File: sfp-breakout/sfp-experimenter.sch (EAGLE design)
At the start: 51 parts, among them IC1 SN65LVDS1DBV, IC2 SN65LVDT2DBV, J1 PJ-002BH-SMT-TR, T1 BC847, T2 BC847, U1 LDO-MCP1825S, X1 PINHD-1X5LOCK, X2 PINHD-1X5LOCK, X3 PINHD-1X4LOCK

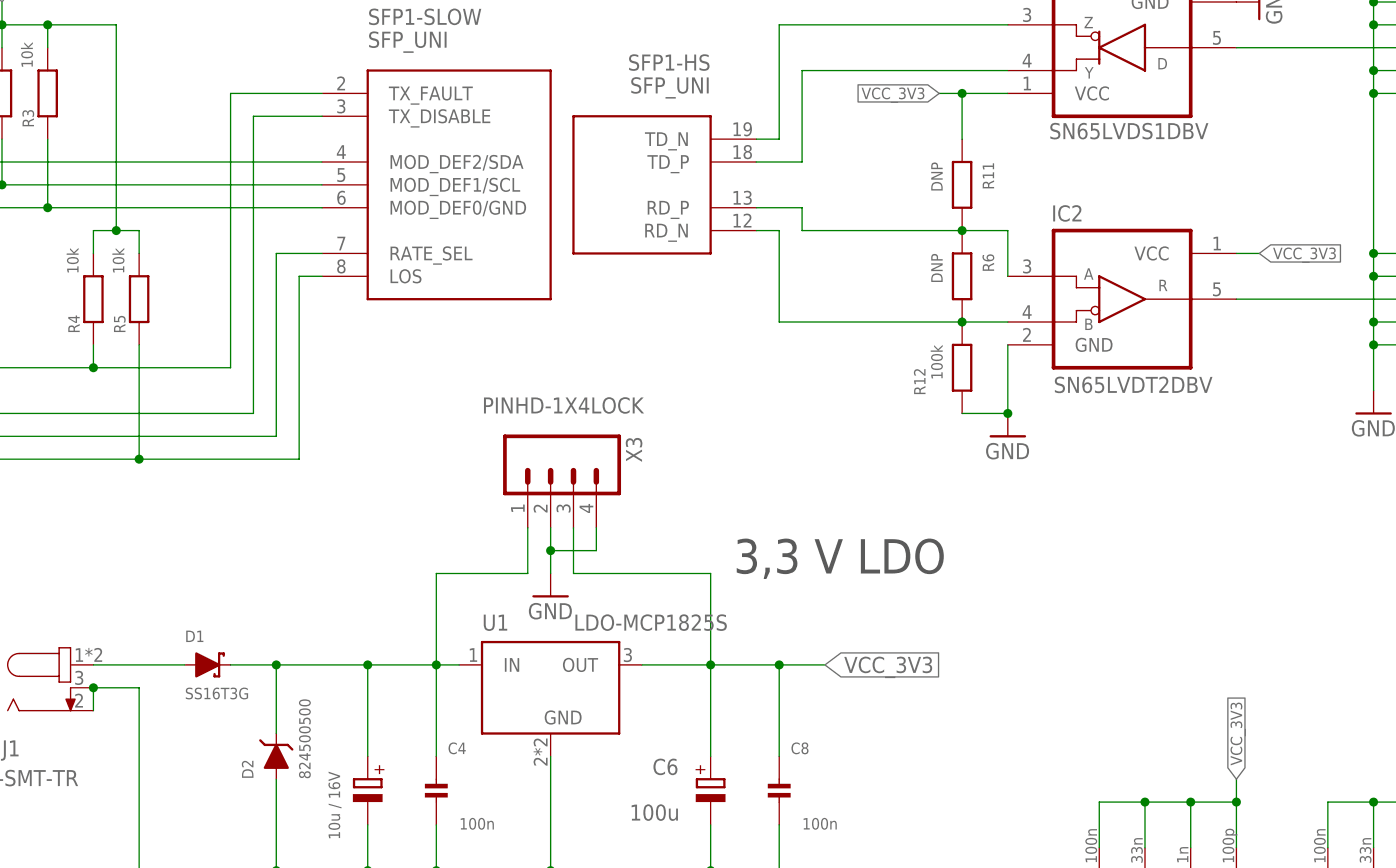
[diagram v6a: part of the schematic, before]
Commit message: sfp-experimenter: update ext BOM attr to newer Digikey format
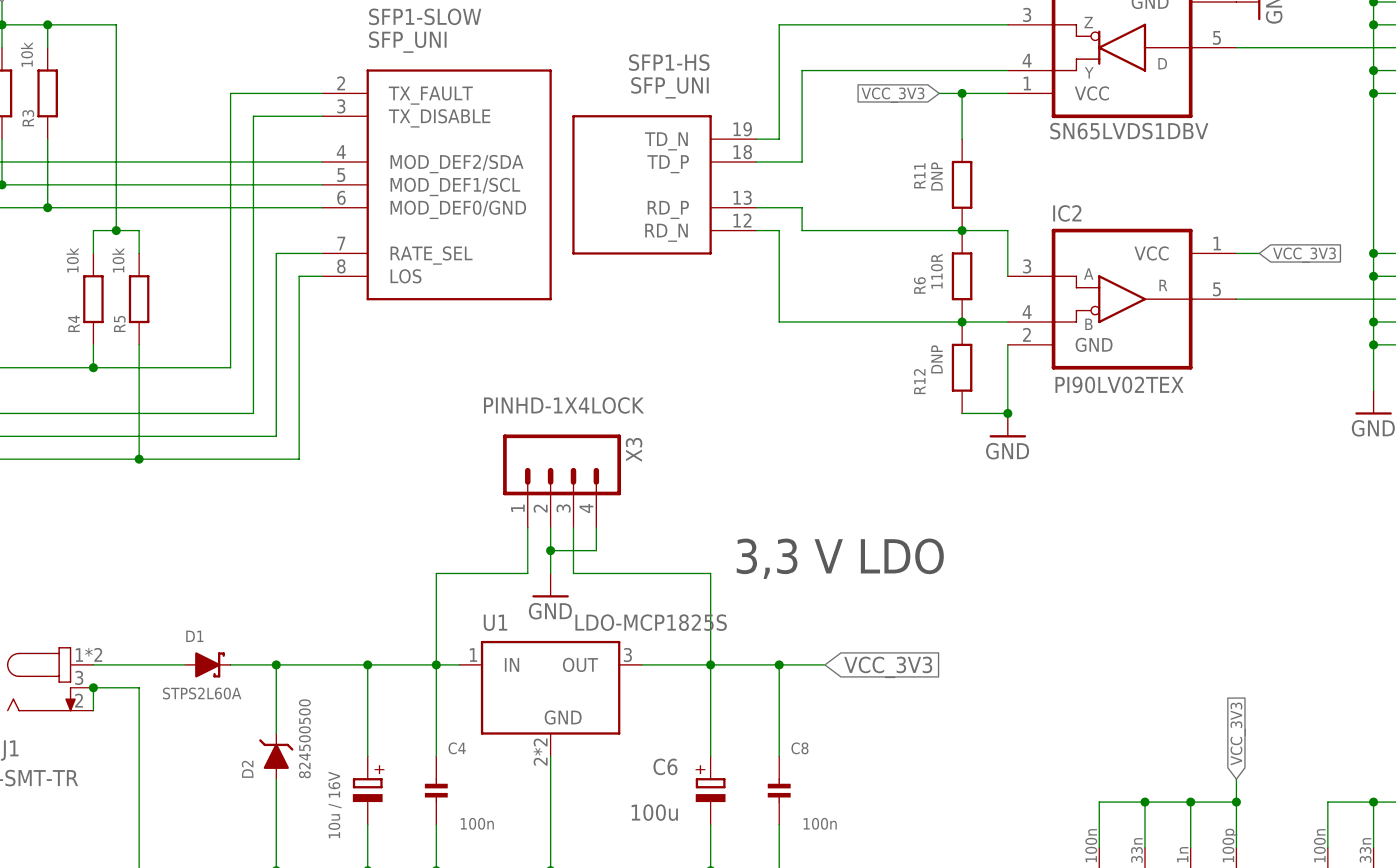
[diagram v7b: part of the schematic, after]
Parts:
- D1: value SS16T3G -> STPS2L60A
- IC2: value SN65LVDT2DBV -> PI90LV02TEX; DATASHEET http://www.ti.com/general/docs/suppproductinfo.tsp?distId=1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 -> https://www.diodes.com/assets/Datasheets/PI90LV02.pdf; LINK https://www.digikey.com/product-detail/en/texas-instruments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 -> https://www.digikey.com/en/products/detail/diodes-incorpora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; MANUFACTURER Texas Instruments -> Diodes Incorporated; MANUFACTURERPARTNUMBER SN65LVDT2DBVR -> PI90LV02TEX; SOURCEPARTNUMBER 296-6896-1-ND -> PI90LV02TEXCT-ND
- R12: value 100k -> DNP; POPULATED TRUE -> FALSE
- R6: value DNP -> 110R; DATASHEET (none) -> https://www.yageo.com/upload/media/product/productsearch/da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; DESCRIPTION NO DESCRIPTION -> RES 110 OHM 1% 1/10W 0603; LINK UNKNOWN LINK -> https://www.digikey.com/en/products/detail/yageo/RC0603FR-1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; MANUFACTURER UNKNOWN MANUFACTURER -> YAGEO; MANUFACTURERPARTNUMBER UNKNOWN MANUFACTURER PART NUMBER -> RC0603FR-13110RL; POPULATED FALSE -> TRUE; ROHSCERTIFICATE UNKNOWN ROHS CERTIFICATE -> ROHS3 Compliant; SOURCE UNKNOWN SOURCE -> DIGIKEY; SOURCEPARTNUMBER UNKNOWN SOURCE PART NUMBER -> 13-RC0603FR-13110RLCT-ND
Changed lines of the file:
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@@
 <part name="GND10" library="sfp-experimenter" deviceset="GND" device=""/>
 <part name="GND13" library="sfp-experimenter" deviceset="GND" device=""/>
-<part name="IC2" library="sfp-experimenter" deviceset="SN65LVDT2" device="DBV" value="SN65LVDT2DBV">
+<part name="IC2" library="sfp-experimenter" deviceset="SN65LVDT2" device="DBV" value="PI90LV02TEX">
 <attribute name="CLASS" value="IC"/>
-<attribute name="DATASHEET" value="http://www.ti.com/general/docs/suppproductinfo.tsp?distId=10&amp;gotoUrl=http%3A%2F%2Fwww.ti.com%2Flit%2Fgpn%2Fsn65lvds1"/>
+<attribute name="DATASHEET" value="https://www.diodes.com/assets/Datasheets/PI90LV02.pdf"/>
 <attribute name="DESCRIPTION" value="IC RECEIVER 0/1 SOT23-5"/>
-<attribute name="LINK" value="https://www.digikey.com/product-detail/en/texas-instruments/SN65LVDT2DBVR/296-6896-1-ND/371534"/>
-<attribute name="MANUFACTURER" value="Texas Instruments"/>
-<attribute name="MANUFACTURERPARTNUMBER" value="SN65LVDT2DBVR"/>
-<attribute name="POPULATED" value="TRUE"/>
-<attribute name="ROHSCERTIFICATE" value="ROHS3 Compliant"/>
-<attribute name="SOURCE" value="DIGIKEY"/>
-<attribute name="SOURCEPARTNUMBER" value="296-6896-1-ND"/>
+<attribute name="LINK" value="https://www.digikey.com/en/products/detail/diodes-incorporated/PI90LV02TEX/1142813"/>
+<attribute name="MANUFACTURER" value="Diodes Incorporated"/>
+<attribute name="MANUFACTURERPARTNUMBER" value="PI90LV02TEX"/>
+<attribute name="POPULATED" value="TRUE"/>
+<attribute name="ROHSCERTIFICATE" value="ROHS3 Compliant"/>
+<attribute name="SOURCE" value="DIGIKEY"/>
+<attribute name="SOURCEPARTNUMBER" value="PI90LV02TEXCT-ND"/>
 </part>
 <part name="IC1" library="sfp-experimenter" deviceset="SN65LVDS1" device="DBV">
@@
 <attribute name="SOURCEPARTNUMBER" value="MCP1825ST-3302E/DBCT-ND"/>
 </part>
-<part name="D1" library="sfp-experimenter" deviceset="DIODE-SCHOTTKY" device="-SMA" value="SS16T3G">
+<part name="D1" library="sfp-experimenter" deviceset="DIODE-SCHOTTKY" device="-SMA" value="STPS2L60A">
 <attribute name="CLASS" value="DIODE"/>
 <attribute name="DATASHEET" value="https://www.st.com/content/ccc/resource/technical/document/datasheet/b7/ac/e1/7d/2a/e9/4b/e8/CD00003166.pdf/files/CD00003166.pdf/jcr:content/translations/en.CD00003166.pdf"/>
@@
 <attribute name="SOURCEPARTNUMBER" value="SMAJ5.0ABCT-ND"/>
 </part>
-<part name="R6" library="sfp-experimenter" deviceset="RESISTOR" device="_0402" value="DNP">
+<part name="R6" library="sfp-experimenter" deviceset="RESISTOR" device="_0402" value="110R">
 <attribute name="CLASS" value="RESISTOR"/>
-<attribute name="DESCRIPTION" value="NO DESCRIPTION"/>
-<attribute name="LINK" value="UNKNOWN LINK"/>
-<attribute name="MANUFACTURER" value="UNKNOWN MANUFACTURER"/>
-<attribute name="MANUFACTURERPARTNUMBER" value="UNKNOWN MANUFACTURER PART NUMBER"/>
-<attribute name="POPULATED" value="FALSE"/>
-<attribute name="ROHSCERTIFICATE" value="UNKNOWN ROHS CERTIFICATE"/>
-<attribute name="SOURCE" value="UNKNOWN SOURCE"/>
-<attribute name="SOURCEPARTNUMBER" value="UNKNOWN SOURCE PART NUMBER"/>
+<attribute name="DATASHEET" value="https://www.yageo.com/upload/media/product/productsearch/datasheet/rchip/PYu-RC_Group_51_RoHS_L_12.pdf"/>
+<attribute name="DESCRIPTION" value="RES 110 OHM 1% 1/10W 0603"/>
+<attribute name="LINK" value="https://www.digikey.com/en/products/detail/yageo/RC0603FR-13110RL/14286378"/>
+<attribute name="MANUFACTURER" value="YAGEO"/>
+<attribute name="MANUFACTURERPARTNUMBER" value="RC0603FR-13110RL"/>
+<attribute name="POPULATED" value="TRUE"/>
+<attribute name="ROHSCERTIFICATE" value="ROHS3 Compliant"/>
+<attribute name="SOURCE" value="DIGIKEY"/>
+<attribute name="SOURCEPARTNUMBER" value="13-RC0603FR-13110RLCT-ND"/>
 </part>
 <part name="X3" library="sfp-experimenter" deviceset="PINHD-1X4" device="LOCK">
@@
 </part>
 <part name="GND22" library="sfp-experimenter" deviceset="GND" device=""/>
-<part name="R12" library="rc-sysmocom" deviceset="RESISTOR" device="_0603" value="100k">
+<part name="R12" library="rc-sysmocom" deviceset="RESISTOR" device="_0603" value="DNP">
 <attribute name="CLASS" value="RESISTOR"/>
 <attribute name="DATASHEET" value="https://www.koaspeer.com/pdfs/RK73H.pdf"/>
@@
 <attribute name="MANUFACTURER" value="KOA Speer Electronics, Inc."/>
 <attribute name="MANUFACTURERPARTNUMBER" value="RK73H1JTTD1003F"/>
-<attribute name="POPULATED" value="TRUE"/>
+<attribute name="POPULATED" value="FALSE"/>
 <attribute name="ROHSCERTIFICATE" value="ROHS3 Compliant"/>
 <attribute name="SOURCE" value="DIGIKEY"/>
@@
 <attribute name="NAME" x="154.686" y="135.636" size="1.778" layer="95" ratio="10"/>
 <attribute name="VALUE" x="154.94" y="116.586" size="1.778" layer="96" ratio="10"/>
-<attribute name="DESCRIPTION" x="162.56" y="127" size="1.27" layer="96" display="off"/>
-<attribute name="MANUFACTURER" x="162.56" y="127" size="1.27" layer="96" display="off"/>
-<attribute name="MANUFACTURERPARTNUMBER" x="162.56" y="127" size="1.27" layer="96" display="off"/>
-<attribute name="SOURCE" x="162.56" y="127" size="1.27" layer="96" display="off"/>
-<attribute name="SOURCEPARTNUMBER" x="162.56" y="127" size="1.27" layer="96" display="off"/>
-<attribute name="ROHSCERTIFICATE" x="162.56" y="127" size="1.27" layer="96" display="off"/>
-<attribute name="POPULATED" x="162.56" y="127" size="1.27" layer="96" display="off"/>
-<attribute name="CLASS" x="162.56" y="127" size="1.27" layer="96" display="off"/>
-<attribute name="LINK" x="162.56" y="127" size="1.27" layer="96" display="off"/>
+<attribute name="DESCRIPTION" x="162.56" y="127" size="1.778" layer="96" rot="R270" display="off"/>
+<attribute name="MANUFACTURER" x="162.56" y="127" size="1.778" layer="96" rot="R270" display="off"/>
+<attribute name="MANUFACTURERPARTNUMBER" x="162.56" y="127" size="1.778" layer="96" rot="R270" display="off"/>
+<attribute name="SOURCE" x="162.56" y="127" size="1.778" layer="96" rot="R270" display="off"/>
+<attribute name="SOURCEPARTNUMBER" x="162.56" y="127" size="1.778" layer="96" rot="R270" display="off"/>
+<attribute name="ROHSCERTIFICATE" x="162.56" y="127" size="1.778" layer="96" rot="R270" display="off"/>
+<attribute name="POPULATED" x="162.56" y="127" size="1.778" layer="96" rot="R270" display="off"/>
+<attribute name="CLASS" x="162.56" y="127" size="1.778" layer="96" rot="R270" display="off"/>
+<attribute name="LINK" x="162.56" y="127" size="1.778" layer="96" rot="R270" display="off"/>
 </instance>
 <instance part="IC1" gate="A" x="162.56" y="154.94" smashed="yes" rot="R180">
@@
 <attribute name="LINK" x="99.06" y="83.82" size="1.778" layer="96" display="off"/>
 </instance>
-<instance part="D1" gate="G$1" x="60.96" y="86.36">
+<instance part="D1" gate="G$1" x="60.96" y="86.36" smashed="yes">
 <attribute name="DESCRIPTION" x="60.96" y="86.36" size="1.778" layer="96" display="off"/>
 <attribute name="MANUFACTURER" x="60.96" y="86.36" size="1.778" layer="96" display="off"/>
@@
 <attribute name="CLASS" x="60.96" y="86.36" size="1.778" layer="96" display="off"/>
 <attribute name="LINK" x="60.96" y="86.36" size="1.778" layer="96" display="off"/>
+<attribute name="NAME" x="58.42" y="88.9" size="1.27" layer="95"/>
+<attribute name="VALUE" x="55.88" y="82.55" size="1.27" layer="96"/>
 </instance>
 <instance part="D2" gate="G$1" x="68.58" y="76.2" rot="R90">
@@
 <attribute name="LINK" x="68.58" y="76.2" size="1.778" layer="96" display="off"/>
 </instance>
-<instance part="R6" gate="G$1" x="144.78" y="129.54" rot="R270">
+<instance part="R6" gate="G$1" x="144.78" y="129.54" smashed="yes" rot="R270">
 <attribute name="DESCRIPTION" x="144.78" y="129.54" size="1.778" layer="96" display="off"/>
 <attribute name="MANUFACTURER" x="144.78" y="129.54" size="1.778" layer="96" display="off"/>
@@
 <attribute name="CLASS" x="144.78" y="129.54" size="1.778" layer="96" display="off"/>
 <attribute name="LINK" x="144.78" y="129.54" size="1.778" layer="96" display="off"/>
+<attribute name="NAME" x="139.446" y="129.54" size="1.27" layer="95" rot="R270"/>
+<attribute name="VALUE" x="141.351" y="132.08" size="1.27" layer="96" rot="R270"/>
 </instance>
 <instance part="X3" gate="G$1" x="99.06" y="109.22" smashed="yes" rot="R270">
@@
 <attribute name="LINK" x="144.78" y="119.38" size="1.778" layer="96" display="off"/>
 </instance>
-<instance part="R11" gate="G$1" x="144.78" y="139.7" rot="R270">
+<instance part="R11" gate="G$1" x="144.78" y="139.7" smashed="yes" rot="R270">
 <attribute name="DESCRIPTION" x="144.78" y="139.7" size="1.778" layer="96" display="off"/>
 <attribute name="MANUFACTURER" x="144.78" y="139.7" size="1.778" layer="96" display="off"/>
@@
 <attribute name="CLASS" x="144.78" y="139.7" size="1.778" layer="96" display="off"/>
 <attribute name="LINK" x="144.78" y="139.7" size="1.778" layer="96" display="off"/>
+<attribute name="NAME" x="139.446" y="142.24" size="1.27" layer="95" rot="R270"/>
+<attribute name="VALUE" x="141.351" y="142.24" size="1.27" layer="96" rot="R270"/>
 </instance>
 <instance part="M1" gate="G$1" x="167.64" y="33.02"/>

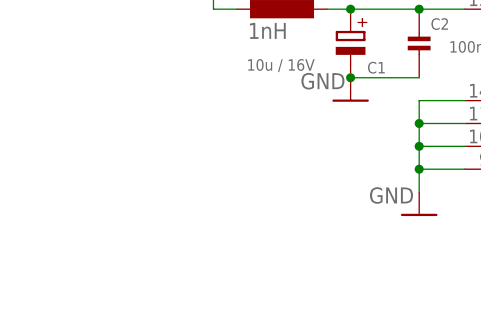
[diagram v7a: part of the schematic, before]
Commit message: sfp-experimenter: insert main fiducials
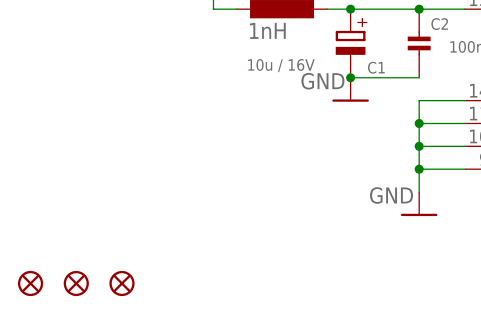
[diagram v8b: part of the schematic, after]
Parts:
- added FID1, FID2, FID3: FIDUCIAL1X2.5, microbuilder:FIDUCIAL1X2.5
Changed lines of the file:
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@@
 <layer number="99" name="position" color="7" fill="9" visible="no" active="yes"/>
 <layer number="100" name="Muster" color="7" fill="1" visible="no" active="no"/>
+<layer number="101" name="Patch_Top" color="12" fill="4" visible="yes" active="yes"/>
+<layer number="102" name="Mittellin" color="7" fill="1" visible="yes" active="yes"/>
+<layer number="103" name="Stiffner" color="7" fill="1" visible="yes" active="yes"/>
+<layer number="104" name="Name" color="7" fill="1" visible="yes" active="yes"/>
 <layer number="105" name="Beschreib" color="9" fill="1" visible="no" active="no"/>
 <layer number="106" name="BGA-Top" color="4" fill="1" visible="no" active="no"/>
 <layer number="107" name="BD-Top" color="5" fill="1" visible="no" active="no"/>
+<layer number="108" name="tBridges" color="7" fill="1" visible="yes" active="yes"/>
+<layer number="109" name="tBPL" color="7" fill="1" visible="yes" active="yes"/>
+<layer number="110" name="bBPL" color="7" fill="1" visible="yes" active="yes"/>
+<layer number="111" name="MPL" color="7" fill="1" visible="yes" active="yes"/>
 <layer number="112" name="Laser Beschriftung-2" color="15" fill="0" visible="no" active="no"/>
 <layer number="113" name="Laser Schnitt" color="12" fill="1" visible="no" active="no"/>
@@
 <layer number="115" name="Laser Bohrungen" color="9" fill="1" visible="no" active="no"/>
 <layer number="118" name="Rect_Pads" color="7" fill="1" visible="no" active="no"/>
+<layer number="121" name="sName" color="7" fill="1" visible="yes" active="yes"/>
+<layer number="122" name="_bPlace" color="7" fill="1" visible="yes" active="yes"/>
+<layer number="125" name="_tNames" color="7" fill="1" visible="yes" active="yes"/>
+<layer number="126" name="_bNames" color="7" fill="1" visible="yes" active="yes"/>
+<layer number="127" name="_tValues" color="7" fill="1" visible="yes" active="yes"/>
+<layer number="128" name="_bValues" color="7" fill="1" visible="yes" active="yes"/>
 <layer number="133" name="Ritzung" color="1" fill="0" visible="no" active="no"/>
 <layer number="134" name="Fräsung" color="2" fill="0" visible="no" active="no"/>
+<layer number="144" name="Drill_legend" color="7" fill="1" visible="yes" active="yes"/>
+<layer number="151" name="HeatSink" color="7" fill="1" visible="yes" active="yes"/>
+<layer number="152" name="_bDocu" color="7" fill="1" visible="yes" active="yes"/>
 <layer number="200" name="200bmp" color="1" fill="10" visible="no" active="no"/>
 <layer number="201" name="201bmp" color="2" fill="1" visible="no" active="no"/>
@@
 <layer number="223" name="223bmp" color="24" fill="1" visible="no" active="no"/>
 <layer number="224" name="224bmp" color="25" fill="1" visible="no" active="no"/>
+<layer number="248" name="Housing" color="7" fill="1" visible="yes" active="yes"/>
+<layer number="249" name="Edge" color="7" fill="1" visible="yes" active="yes"/>
 <layer number="250" name="Descript" color="3" fill="1" visible="no" active="no"/>
 <layer number="251" name="SMDround" color="12" fill="11" visible="no" active="no"/>
+<layer number="254" name="cooling" color="7" fill="1" visible="yes" active="yes"/>
 </layers>
 <schematic xreflabel="%F%N/%S.%C%R" xrefpart="/%S.%C%R">
@@
 <attribute name="SOURCEPARTNUMBER" value="U77-A1114-30L1-ND"/>
 </part>
+<part name="FID1" library="microbuilder" deviceset="FIDUCIAL" device="1X2.5"/>
+<part name="FID2" library="microbuilder" deviceset="FIDUCIAL" device="1X2.5"/>
+<part name="FID3" library="microbuilder" deviceset="FIDUCIAL" device="1X2.5"/>
 </parts>
 <sheets>
@@
 </instance>
 <instance part="M1" gate="G$1" x="167.64" y="33.02"/>
+<instance part="FID1" gate="G$1" x="10.16" y="10.16"/>
+<instance part="FID2" gate="G$1" x="15.24" y="10.16"/>
+<instance part="FID3" gate="G$1" x="20.32" y="10.16"/>
 </instances>
 <busses>
